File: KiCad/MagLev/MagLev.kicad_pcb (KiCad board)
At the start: 2 copper layers, 120 x 120 mm, 204 parts, among them J1 FC681465S, J2 Programming header, J4 USB_B_Micro, Q1 ZX5T851GTA, Q10 ZX5T851GTA, Q11 MMBT3904, Q12 AOD442G, Q13 AOD442G, Q14 ZX5T851GTA, Q16 TEMT7000X01, Q18 ZX5T1951GTA, Q2 ZX5T1951GTA, Q3 ZX5T851GTA, Q4 ZX5T1951GTA, Q5 ZX5T1951GTA, Q6 ZX5T851GTA, Q7 ZX5T1951GTA, Q8 ZX5T851GTA, Q9 ZX5T1951GTA, U1 LM324, U10 X, U11 Y, U12 Z, U13 MCP1402, U14 MCP1402, U2 LM324, U3 L78L05_SO8, U4 TL431A, U5 LM393, U6 ATmega328P-A, U8 FT232RL, U9 LM1117MP-5.0, X1 L_Ferrite, X2 L_Ferrite, Y1 L_Ferrite, Y2 L_Ferrite, Y3 J49SMH-16MHz, Y5 L_Ferrite, Y6 L_Ferrite, Y8 L_Ferrite, Y9 L_Ferrite

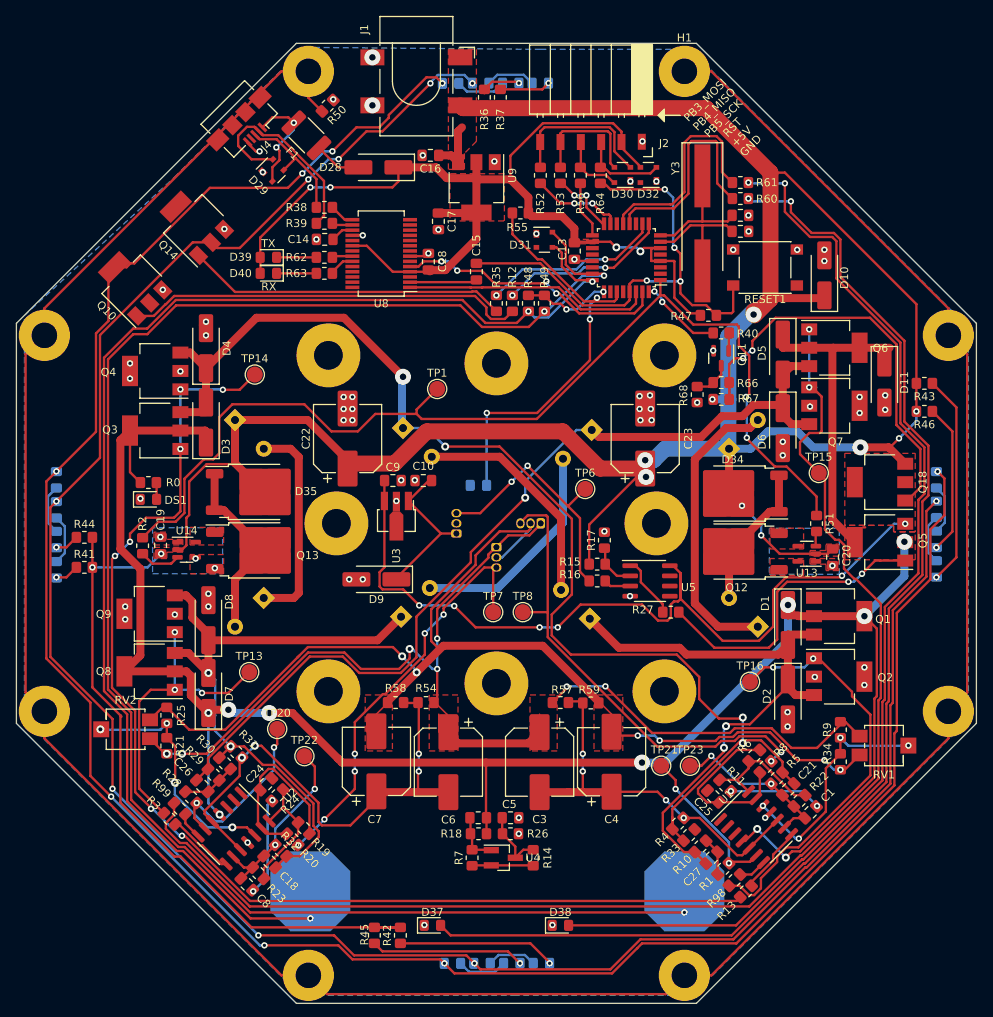
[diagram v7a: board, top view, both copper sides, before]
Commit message: Fix DRC errors.
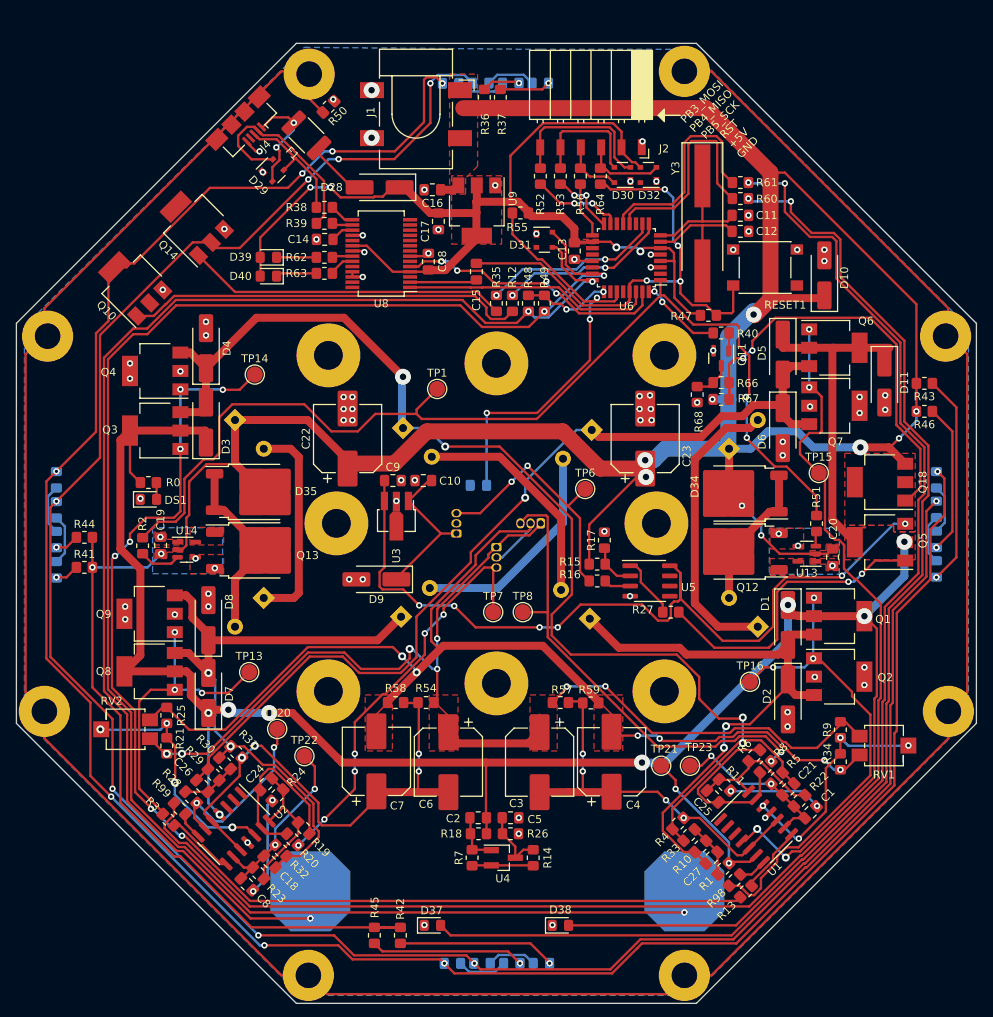
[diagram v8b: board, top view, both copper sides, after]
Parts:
- J4: footprint Connector_USB:USB_Micro-B_Amphenol_10104110_Horizontal -> Maglev_Footprint_Library:USB_Micro-B_Amphenol_10104110_Horizontal_Overhang
- moved C16 4.31 mm to (144.4, 59.9)
- moved J1 4.10 mm to (142.3, 50.5)
- moved U9 2.90 mm to (149.9, 62.5)
- moved D28 2.50 mm to (137.8, 59.6)
- moved J2 0.67 mm to (170.6, 52.6)
- moved H3 0.41 mm to (96.3, 78.2)
- moved H2 0.36 mm to (129.0, 45.5)
- moved H5 0.36 mm to (208.6, 78.2)
- moved D40 0.35 mm to (123.9, 70.7)
- moved R3 0.18 mm to (111.4, 138.7)
- moved R50 0.18 mm to (131.4, 49.5)
- moved J4 0.13 mm to (121.0, 51.9)
- moved R11 0.11 mm to (180.9, 134.3)
- moved R52 0.10 mm to (157.9, 58.2)
- moved R53 0.10 mm to (160.4, 58.2)
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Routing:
- net +5V: track 138.3 -> 130.4 mm
- net Net-(Q1-B): track 52.5 -> 60.1 mm, vias 2 -> 3
- net VCC: track 385.7 -> 380.6 mm
- net /Vref-: track 152.9 -> 148.4 mm
- net GND: track 15.4 -> 19.4 mm, vias 78 -> 84
- net Net-(D13-K): track 283.4 -> 286.3 mm
- net Net-(D21-K): track 277.7 -> 280.6 mm, vias 9 -> 8
- net Earth: track 349.9 -> 347.1 mm
- net Net-(U2B-+): track 63.4 -> 60.9 mm
- net Net-(C25-Pad1): track 16.0 -> 18.1 mm
- net Net-(C27-Pad2): track 4.83 -> 6.83 mm
- net /X1: track 152.6 -> 150.8 mm
- net Net-(C24-Pad1): track 17.0 -> 18.2 mm
- net Net-(R3-Pad2): track 8.90 -> 8.12 mm
- net Net-(Q6-B): track 168.0 -> 167.2 mm
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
